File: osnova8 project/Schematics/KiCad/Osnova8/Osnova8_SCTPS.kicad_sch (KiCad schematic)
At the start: 12 parts, among them U16 74LS670, U17 74LS374, U18 74LS541, U33 74LS541, U34 74LS541, U40 74LS161

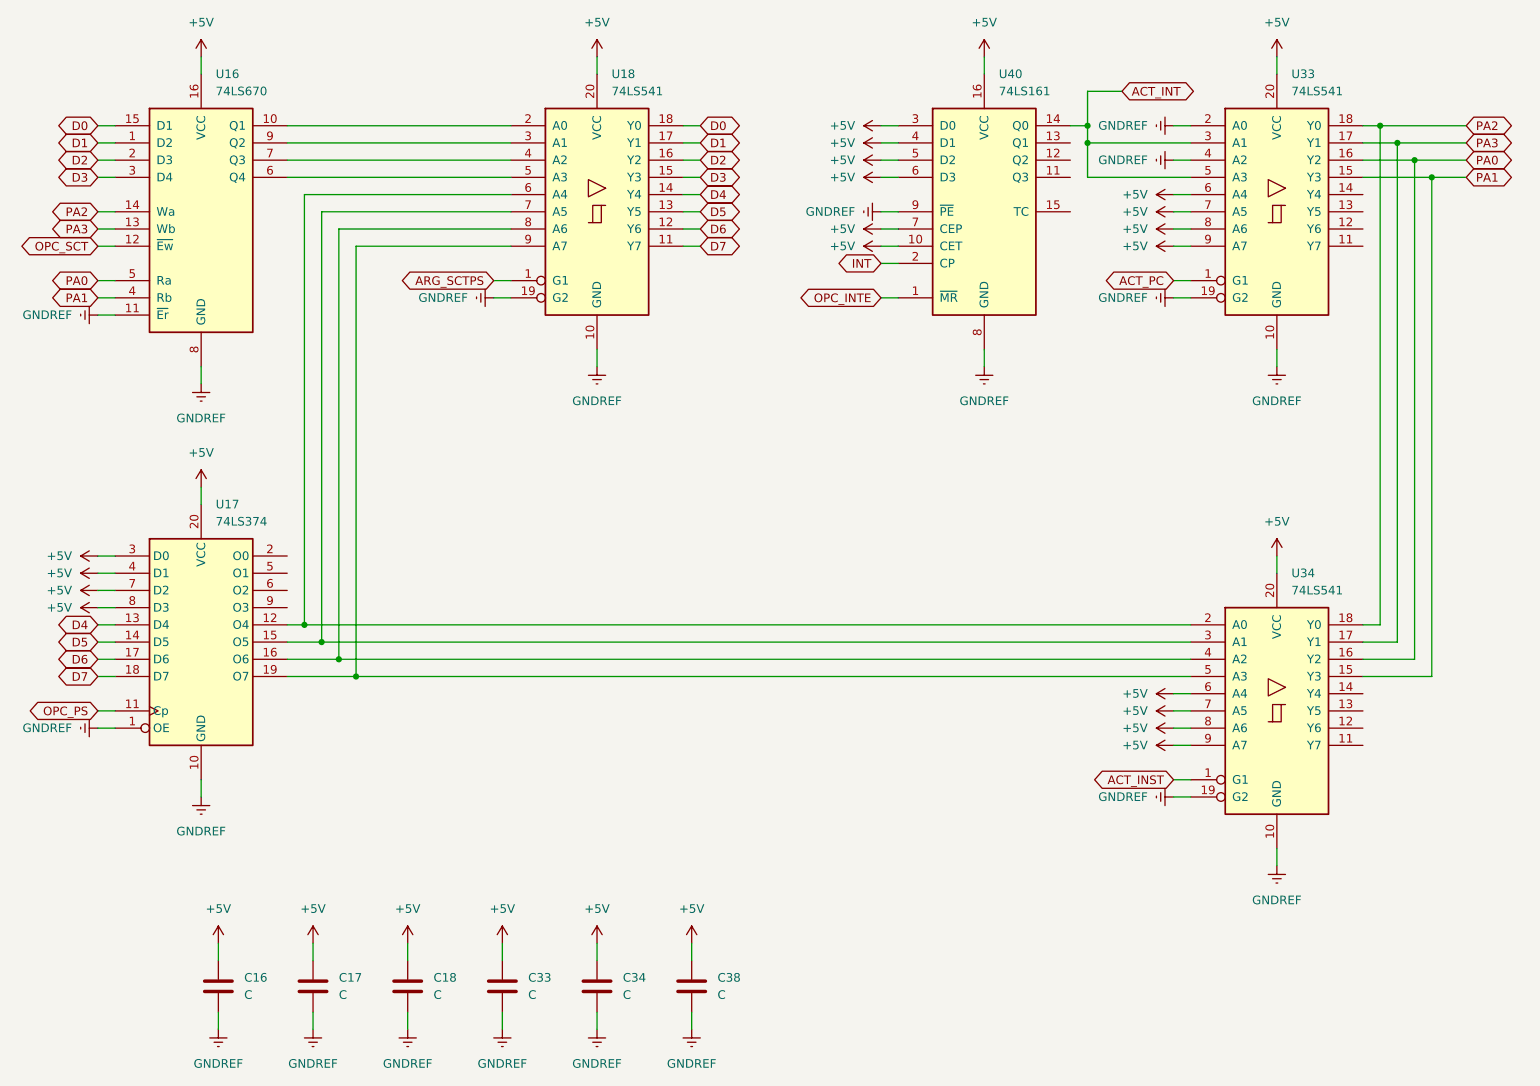
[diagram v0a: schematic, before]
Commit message: updated schematics
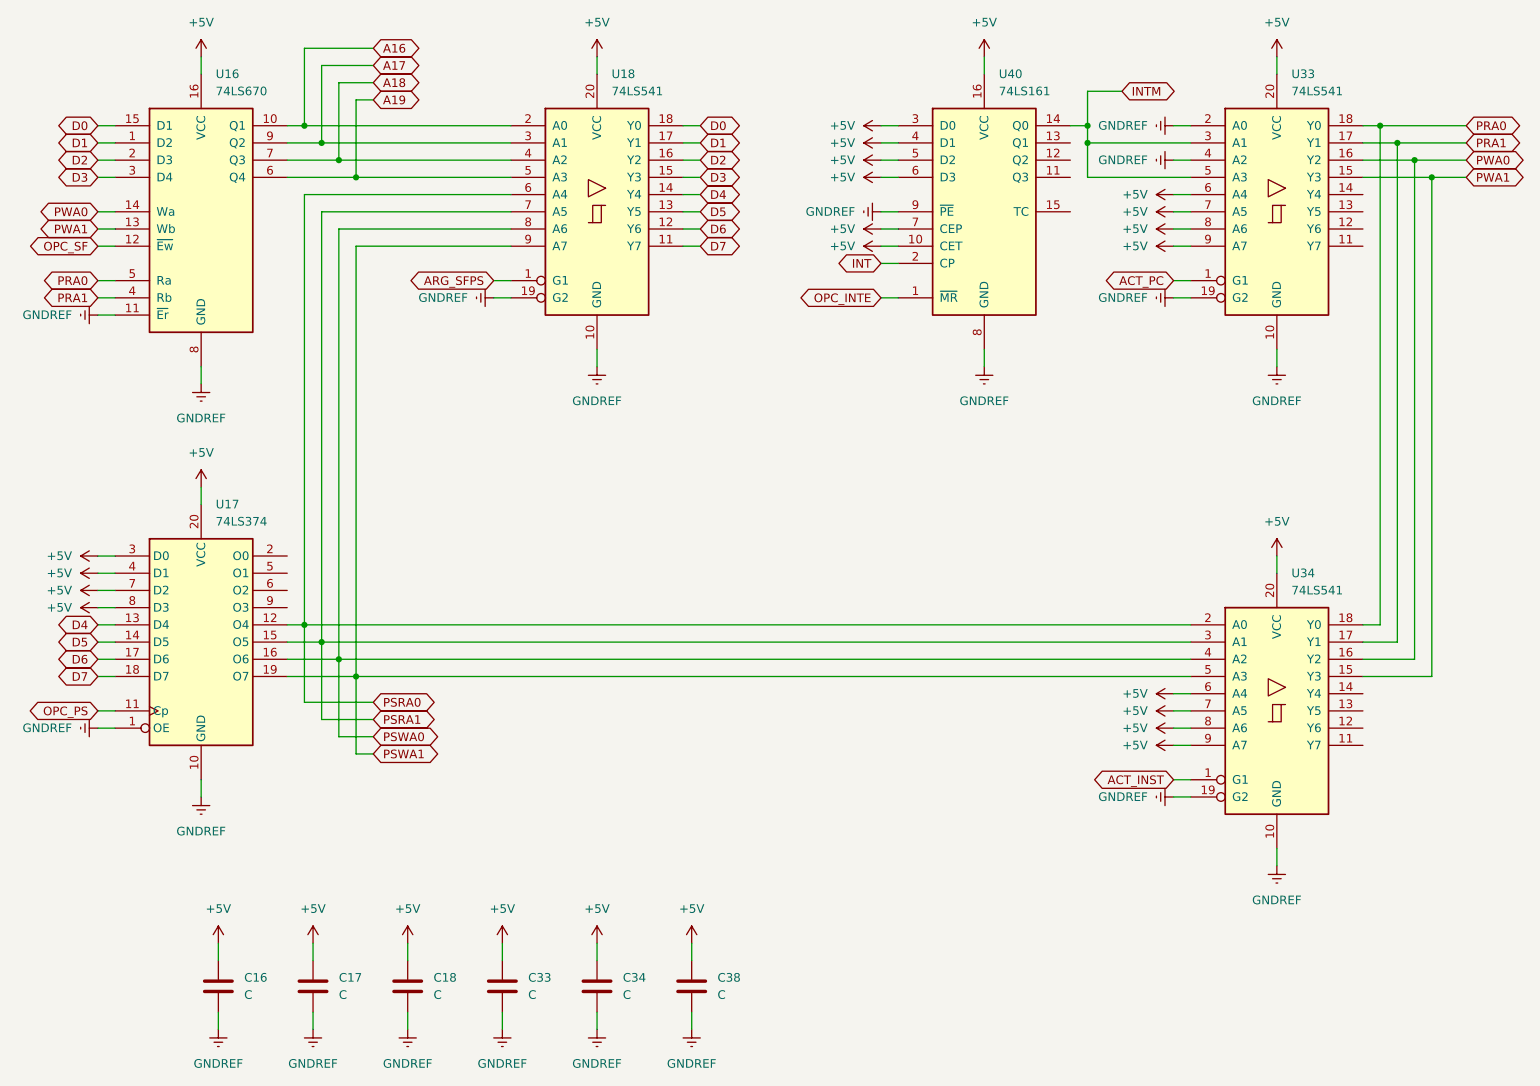
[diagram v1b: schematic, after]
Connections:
- net PSRA0: now reaches U17.12 (O4), U18.6 (A4), U34.2 (A0)
- net PSRA1: now reaches U17.15 (O5), U18.7 (A5), U34.3 (A1)
- net PSWA0: now reaches U17.16 (O6), U18.8 (A6), U34.4 (A2)
- net PSWA1: now reaches U17.19 (O7), U18.9 (A7), U34.5 (A3)
- net A16: now reaches U16.10 (Q1), U18.2 (A0)
- net A17: now reaches U16.9 (Q2), U18.3 (A1)
- net A18: now reaches U16.7 (Q3), U18.4 (A2)
- net A19: now reaches U16.6 (Q4), U18.5 (A3)
- net ACT_INT renamed INTM
- net ARG_SCTPS renamed ARG_SFPS
- net OPC_SCT renamed OPC_SF
- net PA0 renamed PWA0
- net PWA0: now also U16.14 (Wa); no longer U16.5 (Ra)
- net PA1 renamed PWA1
- net PWA1: now also U16.13 (Wb); no longer U16.4 (Rb)
- net PA2 renamed PRA0
- net PRA0: now also U16.5 (Ra); no longer U16.14 (Wa)
- net PA3 renamed PRA1
- net PRA1: now also U16.4 (Rb); no longer U16.13 (Wb)
